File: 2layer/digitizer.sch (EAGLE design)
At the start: 60 parts, among them IC1 FT601QQFN76, X1 SMA-142-0711-881/886, X2 SMA-142-0711-881/886

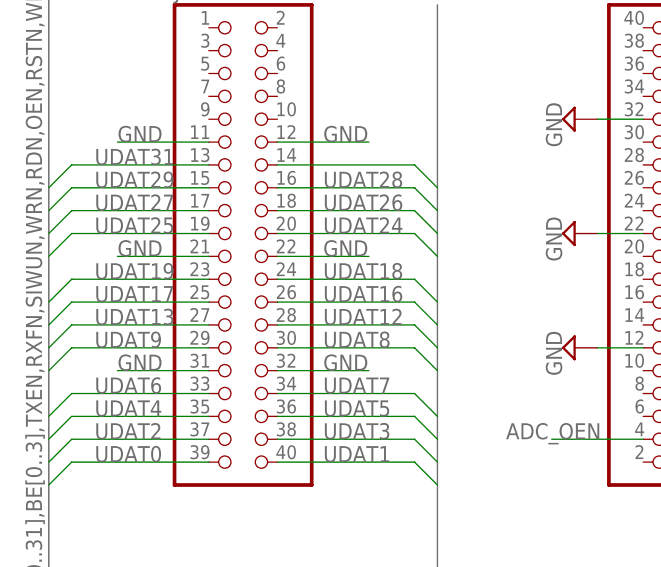
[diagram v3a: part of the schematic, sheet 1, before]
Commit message: autorouter sucks, trying manual
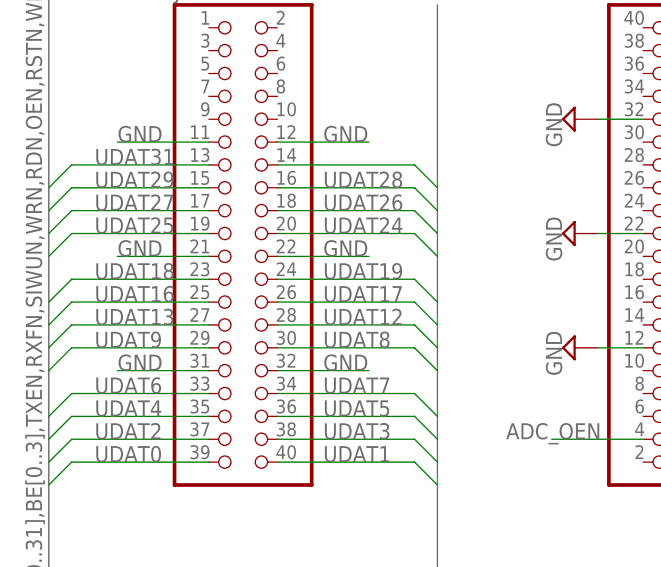
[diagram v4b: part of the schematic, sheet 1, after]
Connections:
- net UDAT16: now also JP2.25; no longer JP2.26
- net UDAT17: now also JP2.26; no longer JP2.25
- net UDAT18: now also JP2.23; no longer JP2.24
- net UDAT19: now also JP2.24; no longer JP2.23
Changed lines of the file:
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@@
 <net name="UDAT16" class="0">
 <segment>
-<pinref part="JP2" gate="A" pin="26"/>
-<wire x1="-76.2" y1="10.16" x2="-78.74" y2="12.7" width="0.1524" layer="91"/>
-<wire x1="-78.74" y1="12.7" x2="-93.98" y2="12.7" width="0.1524" layer="91"/>
-<label x="-88.9" y="12.7" size="1.778" layer="95"/>
+<pinref part="JP2" gate="A" pin="25"/>
+<wire x1="-119.38" y1="10.16" x2="-116.84" y2="12.7" width="0.1524" layer="91"/>
+<wire x1="-116.84" y1="12.7" x2="-101.6" y2="12.7" width="0.1524" layer="91"/>
+<label x="-114.3" y="12.7" size="1.778" layer="95"/>
 </segment>
 </net>
@@
 </segment>
 </net>
-<net name="UDAT17" class="0">
-<segment>
-<pinref part="JP2" gate="A" pin="25"/>
-<wire x1="-119.38" y1="10.16" x2="-116.84" y2="12.7" width="0.1524" layer="91"/>
-<wire x1="-116.84" y1="12.7" x2="-101.6" y2="12.7" width="0.1524" layer="91"/>
-<label x="-114.3" y="12.7" size="1.778" layer="95"/>
-</segment>
-</net>
 <net name="UDAT18" class="0">
+<segment>
+<pinref part="JP2" gate="A" pin="23"/>
+<wire x1="-119.38" y1="12.7" x2="-116.84" y2="15.24" width="0.1524" layer="91"/>
+<wire x1="-116.84" y1="15.24" x2="-101.6" y2="15.24" width="0.1524" layer="91"/>
+<label x="-114.3" y="15.24" size="1.778" layer="95"/>
+</segment>
+</net>
+<net name="UDAT19" class="0">
+<segment>
+<pinref part="JP1" gate="A" pin="24"/>
+<wire x1="-76.2" y1="78.74" x2="-78.74" y2="81.28" width="0.1524" layer="91"/>
+<wire x1="-78.74" y1="81.28" x2="-93.98" y2="81.28" width="0.1524" layer="91"/>
+<label x="-88.9" y="81.28" size="1.778" layer="95"/>
+</segment>
 <segment>
 <pinref part="JP2" gate="A" pin="24"/>
@@
 <wire x1="-78.74" y1="15.24" x2="-93.98" y2="15.24" width="0.1524" layer="91"/>
 <label x="-88.9" y="15.24" size="1.778" layer="95"/>
-</segment>
-</net>
-<net name="UDAT19" class="0">
-<segment>
-<pinref part="JP2" gate="A" pin="23"/>
-<wire x1="-119.38" y1="12.7" x2="-116.84" y2="15.24" width="0.1524" layer="91"/>
-<wire x1="-116.84" y1="15.24" x2="-101.6" y2="15.24" width="0.1524" layer="91"/>
-<label x="-114.3" y="15.24" size="1.778" layer="95"/>
-</segment>
-<segment>
-<pinref part="JP1" gate="A" pin="24"/>
-<wire x1="-76.2" y1="78.74" x2="-78.74" y2="81.28" width="0.1524" layer="91"/>
-<wire x1="-78.74" y1="81.28" x2="-93.98" y2="81.28" width="0.1524" layer="91"/>
-<label x="-88.9" y="81.28" size="1.778" layer="95"/>
 </segment>
 </net>
@@
 </segment>
 </net>
+<net name="UDAT17" class="0">
+<segment>
+<pinref part="JP2" gate="A" pin="26"/>
+<wire x1="-76.2" y1="10.16" x2="-78.74" y2="12.7" width="0.1524" layer="91"/>
+<wire x1="-78.74" y1="12.7" x2="-93.98" y2="12.7" width="0.1524" layer="91"/>
+<label x="-88.9" y="12.7" size="1.778" layer="95"/>
+</segment>
+</net>

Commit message: routing routing routing....
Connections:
- net SFT_RSTN: now also JP4.20; no longer JP3.40
- net SFT_WKPN: now also JP4.26; no longer JP3.38
- net UDAT19: no longer JP1.24
- net UDAT21: now also JP1.20
- net UDAT23: now also JP1.17; no longer JP1.20
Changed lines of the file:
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@@
 <instance part="JP4" gate="A" x="-48.26" y="17.78" rot="R180"/>
 <instance part="SUPPLY8" gate="GND" x="-60.96" y="33.02" rot="R270"/>
-<instance part="SUPPLY9" gate="GND" x="-60.96" y="20.32" rot="R270"/>
+<instance part="SUPPLY9" gate="GND" x="-71.12" y="20.32" rot="R270"/>
 <instance part="SUPPLY10" gate="GND" x="-60.96" y="7.62" rot="R270"/>
 <instance part="SUPPLY28" gate="GND" x="-38.1" y="7.62" rot="R90"/>
@@
 <wire x1="-76.2" y1="-20.32" x2="-76.2" y2="45.72" width="0.762" layer="92"/>
 <wire x1="-119.38" y1="-20.32" x2="-119.38" y2="53.34" width="0.762" layer="92"/>
-<wire x1="-119.38" y1="83.82" x2="-119.38" y2="53.34" width="0.762" layer="92"/>
+<wire x1="-119.38" y1="86.36" x2="-119.38" y2="53.34" width="0.762" layer="92"/>
 <wire x1="-119.38" y1="53.34" x2="-76.2" y2="53.34" width="0.762" layer="92"/>
 <wire x1="-76.2" y1="53.34" x2="-76.2" y2="111.76" width="0.762" layer="92"/>
@@
 <segment>
 <pinref part="JP4" gate="A" pin="22"/>
-<wire x1="-53.34" y1="20.32" x2="-58.42" y2="20.32" width="0.1524" layer="91"/>
+<wire x1="-53.34" y1="20.32" x2="-68.58" y2="20.32" width="0.1524" layer="91"/>
+<pinref part="SUPPLY9" gate="GND" pin="GND"/>
 </segment>
 <segment>
@@
 </segment>
 <segment>
-<pinref part="JP3" gate="A" pin="40"/>
-<wire x1="-63.5" y1="109.22" x2="-53.34" y2="109.22" width="0.1524" layer="91"/>
-<label x="-71.12" y="109.22" size="1.778" layer="95"/>
+<pinref part="JP4" gate="A" pin="20"/>
+<wire x1="-58.42" y1="17.78" x2="-53.34" y2="17.78" width="0.1524" layer="91"/>
+<label x="-58.42" y="17.78" size="1.778" layer="95" rot="R180"/>
 </segment>
 </net>
@@
 </segment>
 <segment>
-<pinref part="JP3" gate="A" pin="38"/>
-<wire x1="-63.5" y1="106.68" x2="-53.34" y2="106.68" width="0.1524" layer="91"/>
-<label x="-71.12" y="106.68" size="1.778" layer="95"/>
+<pinref part="JP4" gate="A" pin="26"/>
+<wire x1="-58.42" y1="25.4" x2="-53.34" y2="25.4" width="0.1524" layer="91"/>
+<label x="-58.42" y="25.4" size="1.778" layer="95" rot="R180"/>
 </segment>
 </net>
@@
 <net name="UDAT19" class="0">
 <segment>
-<pinref part="JP1" gate="A" pin="24"/>
-<wire x1="-76.2" y1="78.74" x2="-78.74" y2="81.28" width="0.1524" layer="91"/>
-<wire x1="-78.74" y1="81.28" x2="-93.98" y2="81.28" width="0.1524" layer="91"/>
-<label x="-88.9" y="81.28" size="1.778" layer="95"/>
-</segment>
-<segment>
 <pinref part="JP2" gate="A" pin="24"/>
 <wire x1="-76.2" y1="12.7" x2="-78.74" y2="15.24" width="0.1524" layer="91"/>
@@
 </segment>
 </net>
-<net name="UDAT22" class="0">
-<segment>
-<pinref part="JP1" gate="A" pin="19"/>
-<wire x1="-119.38" y1="83.82" x2="-116.84" y2="86.36" width="0.1524" layer="91"/>
-<wire x1="-116.84" y1="86.36" x2="-101.6" y2="86.36" width="0.1524" layer="91"/>
-<label x="-114.3" y="86.36" size="1.778" layer="95"/>
-</segment>
-</net>
 <net name="UDAT20" class="0">
 <segment>
@@
 <net name="UDAT23" class="0">
 <segment>
-<pinref part="JP1" gate="A" pin="20"/>
-<wire x1="-76.2" y1="83.82" x2="-78.74" y2="86.36" width="0.1524" layer="91"/>
-<wire x1="-78.74" y1="86.36" x2="-93.98" y2="86.36" width="0.1524" layer="91"/>
-<label x="-88.9" y="86.36" size="1.778" layer="95"/>
+<pinref part="JP1" gate="A" pin="17"/>
+<wire x1="-119.38" y1="86.36" x2="-116.84" y2="88.9" width="0.1524" layer="91"/>
+<wire x1="-116.84" y1="88.9" x2="-101.6" y2="88.9" width="0.1524" layer="91"/>
+<label x="-114.3" y="88.9" size="1.778" layer="95"/>
 </segment>
 </net>
@@
 </segment>
 </net>
+<net name="UDAT22" class="0">
+<segment>
+<pinref part="JP1" gate="A" pin="19"/>
+<wire x1="-119.38" y1="83.82" x2="-116.84" y2="86.36" width="0.1524" layer="91"/>
+<wire x1="-116.84" y1="86.36" x2="-101.6" y2="86.36" width="0.1524" layer="91"/>
+<label x="-114.3" y="86.36" size="1.778" layer="95"/>
+</segment>
+</net>
+<net name="UDAT21" class="0">
+<segment>
+<pinref part="JP1" gate="A" pin="20"/>
+<wire x1="-76.2" y1="83.82" x2="-78.74" y2="86.36" width="0.1524" layer="91"/>
+<wire x1="-78.74" y1="86.36" x2="-93.98" y2="86.36" width="0.1524" layer="91"/>
+<label x="-88.9" y="86.36" size="1.778" layer="95"/>
+</segment>
+</net>
